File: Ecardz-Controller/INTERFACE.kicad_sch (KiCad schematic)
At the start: 41 parts, among them J4 Conn_01x09, J5 Conn_01x01, J6 Conn_01x24, J9 Conn_01x04, Q1 NMOS, Q2 TMBT3904,LM

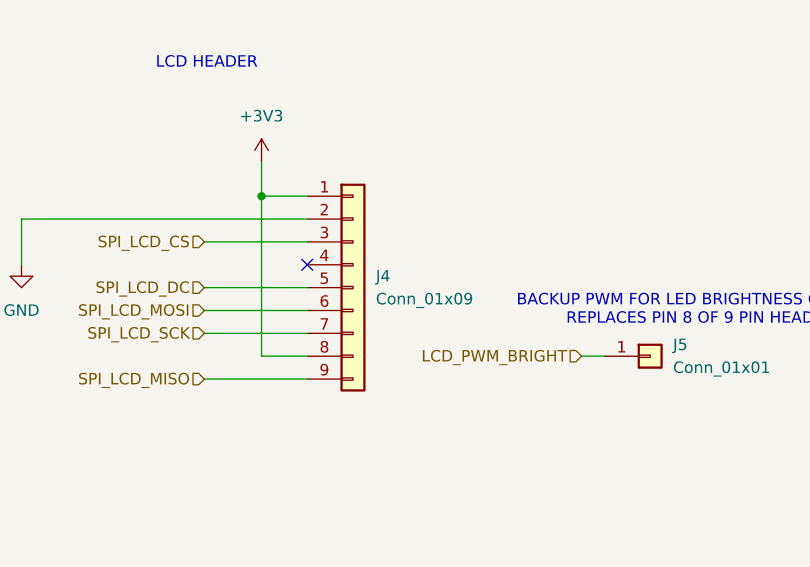
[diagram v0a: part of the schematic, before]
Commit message: changed headers to 90 degree angled headers
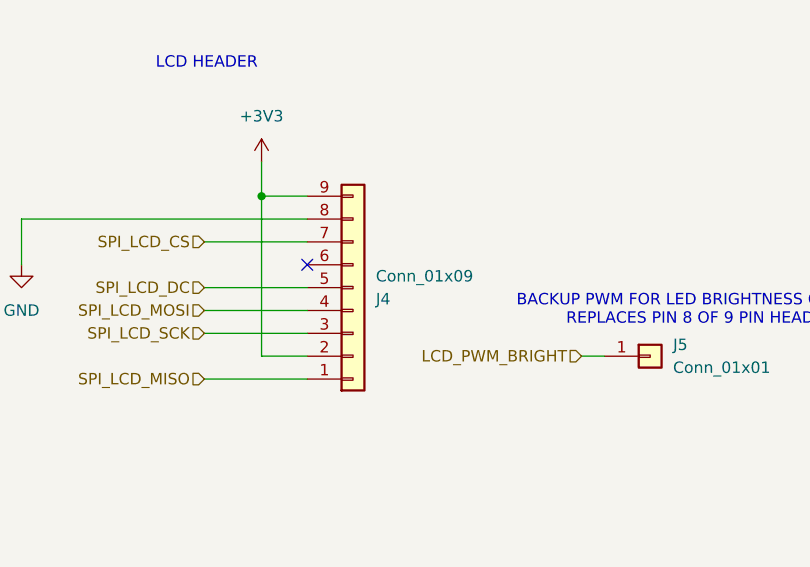
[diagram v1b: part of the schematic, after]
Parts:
- J4: footprint Connector_PinHeader_2.54mm:PinHeader_1x09_P2.54mm_Vertical -> Connector_PinHeader_2.54mm:PinHeader_1x09_P2.54mm_Horizontal
- J5: footprint Connector_PinHeader_2.54mm:PinHeader_1x01_P2.54mm_Vertical -> Connector_PinHeader_2.54mm:PinHeader_1x01_P2.54mm_Horizontal
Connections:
- net +3V3: now also J4.2 (Pin_2), J4.9 (Pin_9); no longer J4.1 (Pin_1), J4.8 (Pin_8)
- net GND: now also J4.8 (Pin_8); no longer J4.2 (Pin_2)
- net SPI_LCD_CS: now also J4.7 (Pin_7); no longer J4.3 (Pin_3)
- net SPI_LCD_MISO: now also J4.1 (Pin_1); no longer J4.9 (Pin_9)
- net SPI_LCD_MOSI: now also J4.4 (Pin_4); no longer J4.6 (Pin_6)
- net SPI_LCD_SCK: now also J4.3 (Pin_3); no longer J4.7 (Pin_7)
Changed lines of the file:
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@@
 	)
 	(symbol
-		(lib_id "Connector_Generic:Conn_01x09")
-		(at 203.2 139.7 0)
-		(unit 1)
-		(exclude_from_sim no)
-		(in_bom yes)
-		(on_board yes)
-		(dnp no)
-		(fields_autoplaced yes)
-		(property "Reference" "J4"
-			(at 205.74 138.4299 0)
-			(effects
-				(font
-					(size 1.27 1.27)
-				)
-				(justify left)
-			)
-		)
-		(property "Value" "Conn_01x09"
-			(at 205.74 140.9699 0)
-			(effects
-				(font
-					(size 1.27 1.27)
-				)
-				(justify left)
-			)
-		)
-		(property "Footprint" "Connector_PinHeader_2.54mm:PinHeader_1x09_P2.54mm_Vertical"
-			(at 203.2 139.7 0)
-			(effects
-				(font
-					(size 1.27 1.27)
-				)
-				(hide yes)
-			)
-		)
-		(property "Datasheet" ""
-			(at 203.2 139.7 0)
-			(effects
-				(font
-					(size 1.27 1.27)
-				)
-				(hide yes)
-			)
-		)
-		(property "Description" "Generic connector, single row, 01x09, script generated (kicad-library-utils/schlib/autogen/connector/)"
-			(at 203.2 139.7 0)
-			(effects
-				(font
-					(size 1.27 1.27)
-				)
-				(hide yes)
-			)
-		)
-		(property "Part Number" "61300911121"
-			(at 203.2 139.7 0)
-			(effects
-				(font
-					(size 1.27 1.27)
-				)
-				(hide yes)
-			)
-		)
-		(pin "1"
-		)
-		(pin "2"
-		)
-		(pin "3"
-		)
-		(pin "5"
-		)
-		(pin "6"
-		)
-		(pin "4"
-		)
-		(pin "9"
-		)
-		(pin "8"
-		)
-		(pin "7"
-		)
-		(instances
-			(project "Ecardz-Controller"
-				(path "/74270717-a116-451e-ac88-5a07ab66056e/c8fd81b3-86d5-41d1-a22c-ff1dbf0b272c"
-					(reference "J4")
-					(unit 1)
-				)
-			)
-		)
-	)
-	(symbol
 		(lib_id "Device:R_US")
 		(at 130.81 60.96 0)
@@
 			)
 		)
-		(property "Footprint" "Connector_PinHeader_2.54mm:PinHeader_1x01_P2.54mm_Vertical"
+		(property "Footprint" "Connector_PinHeader_2.54mm:PinHeader_1x01_P2.54mm_Horizontal"
 			(at 236.22 147.32 0)
 			(effects
@@
 					(unit 1)
 				)
+			)
+		)
+	)
+	(symbol
+		(lib_id "Connector_Generic:Conn_01x09")
+		(at 203.2 139.7 0)
+		(mirror x)
+		(unit 1)
+		(exclude_from_sim no)
+		(in_bom yes)
+		(on_board yes)
+		(dnp no)
+		(property "Reference" "J4"
+			(at 205.74 140.9701 0)
+			(effects
+				(font
+					(size 1.27 1.27)
+				)
+				(justify left)
+			)
+		)
+		(property "Value" "Conn_01x09"
+			(at 205.74 138.4301 0)
+			(effects
+				(font
+					(size 1.27 1.27)
+				)
+				(justify left)
+			)
+		)
+		(property "Footprint" "Connector_PinHeader_2.54mm:PinHeader_1x09_P2.54mm_Horizontal"
+			(at 203.2 139.7 0)
+			(effects
+				(font
+					(size 1.27 1.27)
+				)
+				(hide yes)
+			)
+		)
+		(property "Datasheet" ""
+			(at 203.2 139.7 0)
+			(effects
+				(font
+					(size 1.27 1.27)
+				)
+				(hide yes)
+			)
+		)
+		(property "Description" "Generic connector, single row, 01x09, script generated (kicad-library-utils/schlib/autogen/connector/)"
+			(at 203.2 139.7 0)
+			(effects
+				(font
+					(size 1.27 1.27)
+				)
+				(hide yes)
+			)
+		)
+		(property "Part Number" "61300911121"
+			(at 203.2 139.7 0)
+			(effects
+				(font
+					(size 1.27 1.27)
+				)
+				(hide yes)
+			)
+		)
+		(pin "1"
+		)
+		(pin "2"
+		)
+		(pin "3"
+		)
+		(pin "5"
+		)
+		(pin "6"
+		)
+		(pin "4"
+		)
+		(pin "9"
+		)
+		(pin "8"
+		)
+		(pin "7"
+		)
+		(instances
+			(project "Ecardz-Controller"
+				(path "/74270717-a116-451e-ac88-5a07ab66056e/c8fd81b3-86d5-41d1-a22c-ff1dbf0b272c"
+					(reference "J4")
+					(unit 1)
+				)

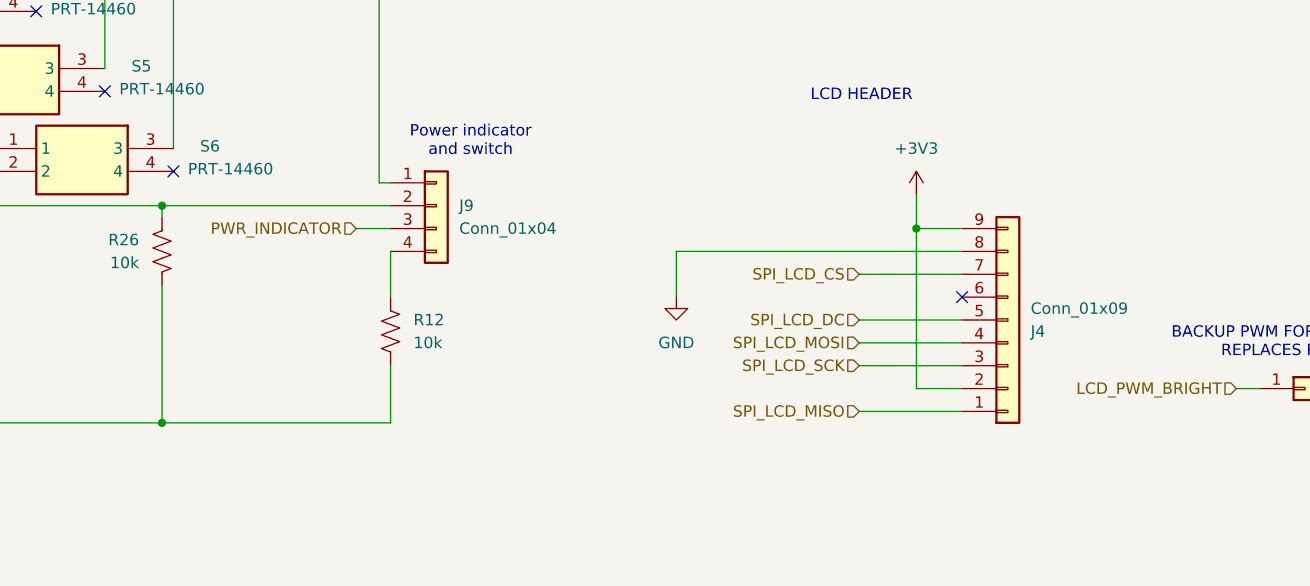
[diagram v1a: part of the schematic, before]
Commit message: moved headers to bottom of board, made J3 DNP
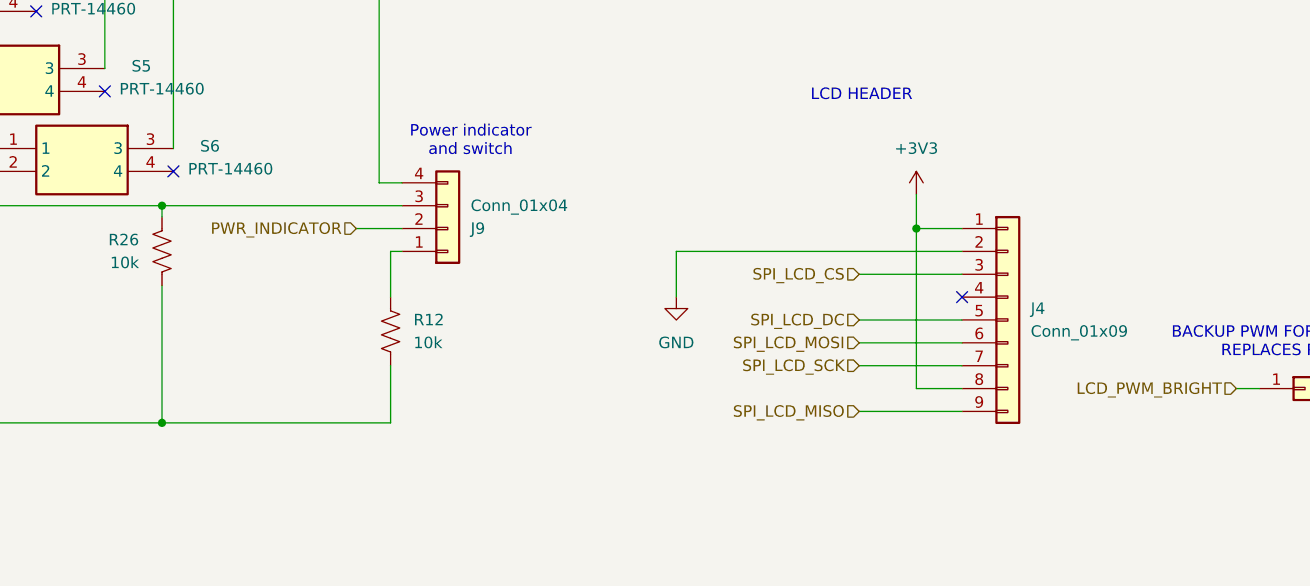
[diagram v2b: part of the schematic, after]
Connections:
- net +3V3: now also J4.1 (Pin_1), J4.8 (Pin_8), J9.4 (Pin_4); no longer J4.2 (Pin_2), J4.9 (Pin_9), J9.1 (Pin_1)
- net BUTTON7: now also J9.3 (Pin_3); no longer J9.2 (Pin_2)
- net GND: now also J4.2 (Pin_2); no longer J4.8 (Pin_8)
- net PWR_INDICATOR: now also J9.2 (Pin_2); no longer J9.3 (Pin_3)
- net SPI_LCD_CS: now also J4.3 (Pin_3); no longer J4.7 (Pin_7)
- net SPI_LCD_MISO: now also J4.9 (Pin_9); no longer J4.1 (Pin_1)
- net SPI_LCD_MOSI: now also J4.6 (Pin_6); no longer J4.4 (Pin_4)
- net SPI_LCD_SCK: now also J4.7 (Pin_7); no longer J4.3 (Pin_3)
- net at R12.1: now also J9.1 (Pin_1); no longer J9.4 (Pin_4)
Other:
- moved on the sheet: J9
